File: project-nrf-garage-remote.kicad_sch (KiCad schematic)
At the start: 4 parts, among them J1 Screw_Terminal_01x02, J2 Screw_Terminal_01x04, Q1 BSS138W, Q2 BSS138W

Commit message: Connect schematic
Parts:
- added H1, H2, H3, H4: MountingHole_Pad, symbol Mechanical:MountingHole_Pad
- added R1: R, Resistor_SMD:R_0603_1608Metric, symbol Device:R
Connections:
- net uc_send: now reaches Q2.1 (G)
- net uc_send: now also J2.1 (Pin_1), R1.1
- net GND: now reaches Q2.2 (S)
- net GND: now also J1.2 (Pin_2), J2.3 (Pin_3), Q1.2 (S), H1.1, H2.1, H3.1, H4.1, R1.2
- net motor_data: now reaches Q2.3 (D)
- net motor_data: now also J1.1 (Pin_1), Q1.1 (G)
- net uc_recv: now reaches J2.2 (Pin_2)
- net uc_recv: now also Q1.3 (D)
- no-connect marks 0 -> 1
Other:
- moved on the sheet: J1, J2, Q1, Q2

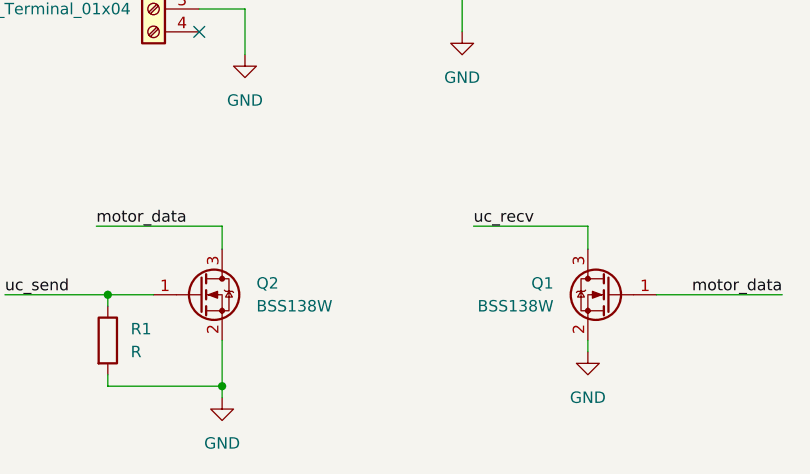
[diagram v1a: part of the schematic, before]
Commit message: Swap mosfet symbols
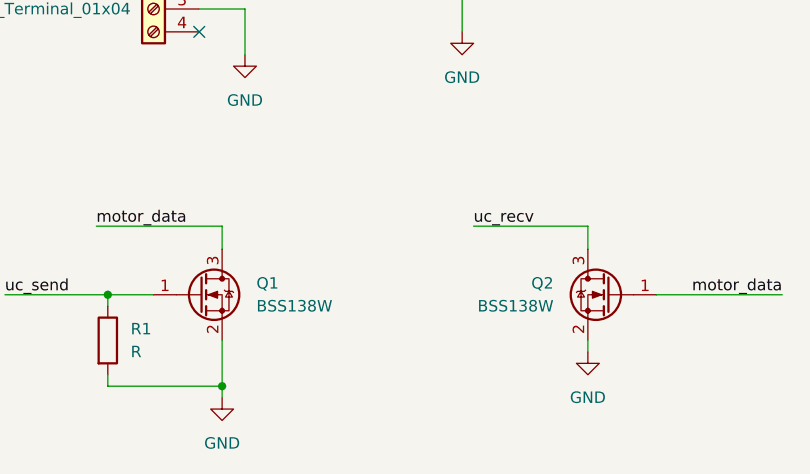
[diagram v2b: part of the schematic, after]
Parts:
- removed Q1, Q2: BSS138W, Package_TO_SOT_SMD:SOT-323_SC-70, symbol Device:Q_NMOS_GSD
- added Q1, Q2: BSS138W, BSS138W:BSS138W, symbol BSS138W:BSS138W
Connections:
- net GND: now also Q1.2 (S), Q2.2 (S)
- net motor_data: now also Q1.3 (D), Q2.1 (G)
- net uc_recv: now also Q2.3 (D)
- net uc_send: now also Q1.1 (G)

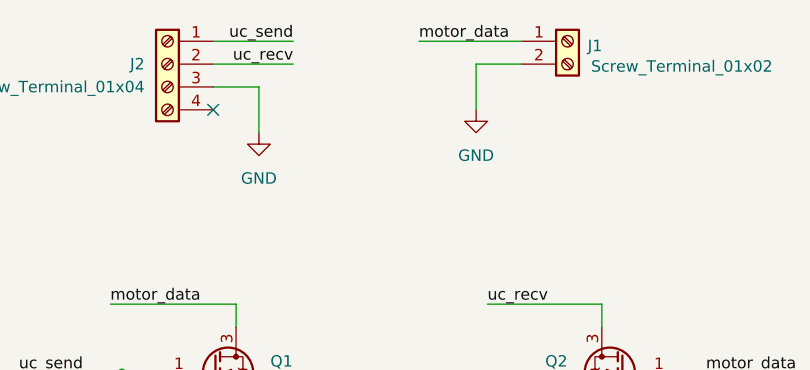
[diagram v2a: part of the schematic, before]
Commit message: Add footprint to mounting holes
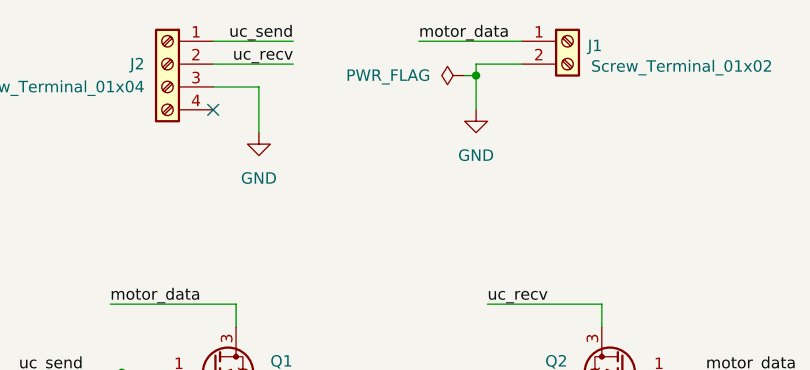
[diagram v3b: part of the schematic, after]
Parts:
- H1, H2, H3, H4: footprint (none) -> MountingHole:MountingHole_2.2mm_M2_ISO14580_Pad
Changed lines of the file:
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@@
+	)
+	(junction
+		(at 74.93 22.86)
+		(diameter 0)
+		(color 0 0 0 0)
 	)
 	(junction
@@
 	(wire
 		(pts
+			(xy 73.66 22.86) (xy 74.93 22.86)
+		)
+		(stroke
+			(width 0)
+			(type default)
+		)
+	)
+	(wire
+		(pts
 			(xy 45.72 24.13) (xy 50.8 24.13)
 		)
@@
 	(wire
 		(pts
+			(xy 74.93 22.86) (xy 74.93 26.67)
+		)
+		(stroke
+			(width 0)
+			(type default)
+		)
+	)
+	(wire
+		(pts
 			(xy 35.56 64.77) (xy 35.56 66.04)
 		)
@@
 	(wire
 		(pts
+			(xy 74.93 21.59) (xy 74.93 22.86)
+		)
+		(stroke
+			(width 0)
+			(type default)
+		)
+	)
+	(wire
+		(pts
 			(xy 144.78 44.45) (xy 154.94 44.45)
 		)
@@
 		(pts
 			(xy 35.56 66.04) (xy 48.26 66.04)
-		)
-		(stroke
-			(width 0)
-			(type default)
-		)
-	)
-	(wire
-		(pts
-			(xy 74.93 21.59) (xy 74.93 26.67)
 		)
 		(stroke
@@
 			)
 		)
-		(property "Footprint" ""
+		(property "Footprint" "MountingHole:MountingHole_2.2mm_M2_ISO14580_Pad"
 			(at 142.24 54.61 0)
 			(effects
@@
 			)
 		)
-		(property "Footprint" ""
+		(property "Footprint" "MountingHole:MountingHole_2.2mm_M2_ISO14580_Pad"
 			(at 142.24 44.45 0)
 			(effects
@@
 	)
 	(symbol
+		(lib_id "power:PWR_FLAG")
+		(at 73.66 22.86 90)
+		(unit 1)
+		(exclude_from_sim no)
+		(in_bom yes)
+		(on_board yes)
+		(dnp no)
+		(fields_autoplaced yes)
+		(property "Reference" "#FLG01"
+			(at 71.755 22.86 0)
+			(effects
+				(font
+					(size 1.27 1.27)
+				)
+				(hide yes)
+			)
+		)
+		(property "Value" "PWR_FLAG"
+			(at 69.85 22.8599 90)
+			(effects
+				(font
+					(size 1.27 1.27)
+				)
+				(justify left)
+			)
+		)
+		(property "Footprint" ""
+			(at 73.66 22.86 0)
+			(effects
+				(font
+					(size 1.27 1.27)
+				)
+				(hide yes)
+			)
+		)
+		(property "Datasheet" "~"
+			(at 73.66 22.86 0)
+			(effects
+				(font
+					(size 1.27 1.27)
+				)
+				(hide yes)
+			)
+		)
+		(property "Description" "Special symbol for telling ERC where power comes from"
+			(at 73.66 22.86 0)
+			(effects
+				(font
+					(size 1.27 1.27)
+				)
+				(hide yes)
+			)
+		)
+		(pin "1"
+		)
+		(instances
+			(project ""
+				(path "/14484fb2-31b8-4fde-a469-eb6264645a81"
+					(reference "#FLG01")
+					(unit 1)
+				)
+			)
+		)
+	)
+	(symbol
 		(lib_id "power:GND")
 		(at 50.8 29.21 0)
@@
 			)
 		)
-		(property "Footprint" ""
+		(property "Footprint" "MountingHole:MountingHole_2.2mm_M2_ISO14580_Pad"
 			(at 142.24 34.29 0)
 			(effects
@@
 			)
 		)
-		(property "Footprint" ""
+		(property "Footprint" "MountingHole:MountingHole_2.2mm_M2_ISO14580_Pad"
 			(at 142.24 24.13 0)
 			(effects

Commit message: Started board placement
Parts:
- R1: value R -> PD
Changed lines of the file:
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@@
 			)
 		)
-		(property "Value" "R"
+		(property "Value" "PD"
 			(at 38.1 62.2299 0)
 			(effects

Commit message: Change the terminals footprint
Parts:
- J1: footprint Conn_Molex_393570002:Molex-393570002-MFG -> TZ022101B000G:TZ022101B000G
- J2: footprint Conn_Molex_393570004:Molex-393570004-MFG -> TZ042101B000G:TZ042101B000G
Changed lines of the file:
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@@
 			)
 		)
-		(property "Footprint" "Conn_Molex_393570004:Molex-393570004-MFG"
+		(property "Footprint" "TZ042101B000G:TZ042101B000G"
 			(at 40.64 21.59 0)
 			(effects
@@
 			)
 		)
-		(property "Footprint" "Conn_Molex_393570002:Molex-393570002-MFG"
+		(property "Footprint" "TZ022101B000G:TZ022101B000G"
 			(at 85.09 19.05 0)
 			(effects

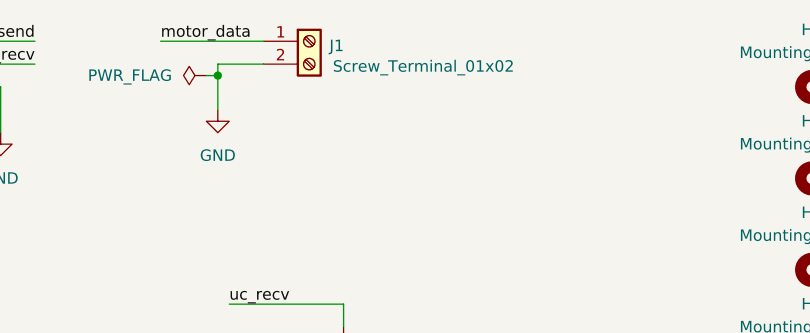
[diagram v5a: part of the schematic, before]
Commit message: Add silkscreen
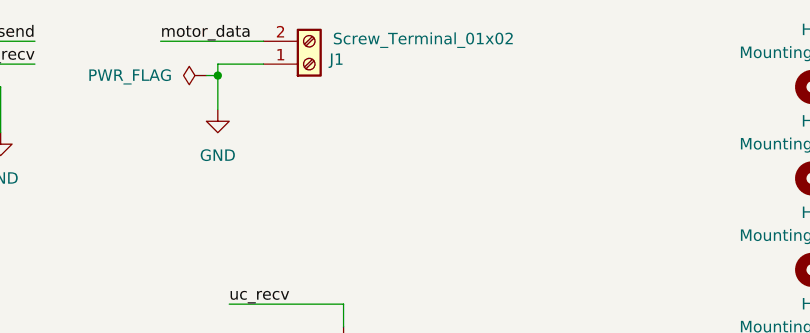
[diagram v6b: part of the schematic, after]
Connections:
- net GND: now also J1.1 (Pin_1); no longer J1.2 (Pin_2)
- net motor_data: now also J1.2 (Pin_2); no longer J1.1 (Pin_1)
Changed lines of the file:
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@@
 	(symbol
 		(lib_id "Connector:Screw_Terminal_01x02")
-		(at 85.09 19.05 0)
+		(at 85.09 21.59 0)
+		(mirror x)
 		(unit 1)
 		(exclude_from_sim no)
@@
 		(dnp no)
 		(property "Reference" "J1"
-			(at 88.138 19.558 0)
+			(at 88.138 21.082 0)
 			(effects
 				(font
@@
 		)
 		(property "Value" "Screw_Terminal_01x02"
-			(at 97.79 21.844 0)
+			(at 97.79 18.796 0)
 			(effects
 				(font
@@
 		)
 		(property "Footprint" "TZ022101B000G:TZ022101B000G"
-			(at 85.09 19.05 0)
+			(at 85.09 21.59 0)
 			(effects
 				(font
@@
 		)
 		(property "Datasheet" "~"
-			(at 85.09 19.05 0)
+			(at 85.09 21.59 0)
 			(effects
 				(font
@@
 		)
 		(property "Description" "Generic screw terminal, single row, 01x02, script generated (kicad-library-utils/schlib/autogen/connector/)"
-			(at 85.09 19.05 0)
+			(at 85.09 21.59 0)
 			(effects
 				(font

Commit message: Update schematic
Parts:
- added R2: PU, Resistor_SMD:R_0603_1608Metric, symbol Device:R
- R1: value PD -> PU
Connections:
- net GND: now also J2.4 (Pin_4); no longer J2.3 (Pin_3), Q1.2 (S), Q2.2 (S), R1.2
- net motor_data: now also Q2.3 (D); no longer Q2.1 (G)
- net uc_recv: now also J2.3 (Pin_3), Q2.2 (S), R1.2; no longer J2.2 (Pin_2), Q2.3 (D)
- net uc_send: now also J2.2 (Pin_2), Q1.2 (S), R2.2; no longer J2.1 (Pin_1), Q1.1 (G), R1.1
- new net VDD: J2.1 (Pin_1), Q1.1 (G), Q2.1 (G), R1.1, R2.1
- no-connect marks 1 -> 0
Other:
- moved on the sheet: J1, J2, Q1, Q2, R1

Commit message: Set do not populate part
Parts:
- R2: now not fitted
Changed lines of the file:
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@@
 		(in_bom yes)
 		(on_board yes)
-		(dnp no)
+		(dnp yes)
 		(fields_autoplaced yes)
 		(property "Reference" "R2"
